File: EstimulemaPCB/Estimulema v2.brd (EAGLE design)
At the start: 150 x 160 mm, 157 parts, among them IC3 74AC14N, IC4 ISO7240S, J1 JUMPERS12MM, J2 J15MM, J3 J_7MM, J4 JUMPERS5MM, J5 JUMPERS7MM, J6 J7MM, K2 HC-06, Q17 TIP48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

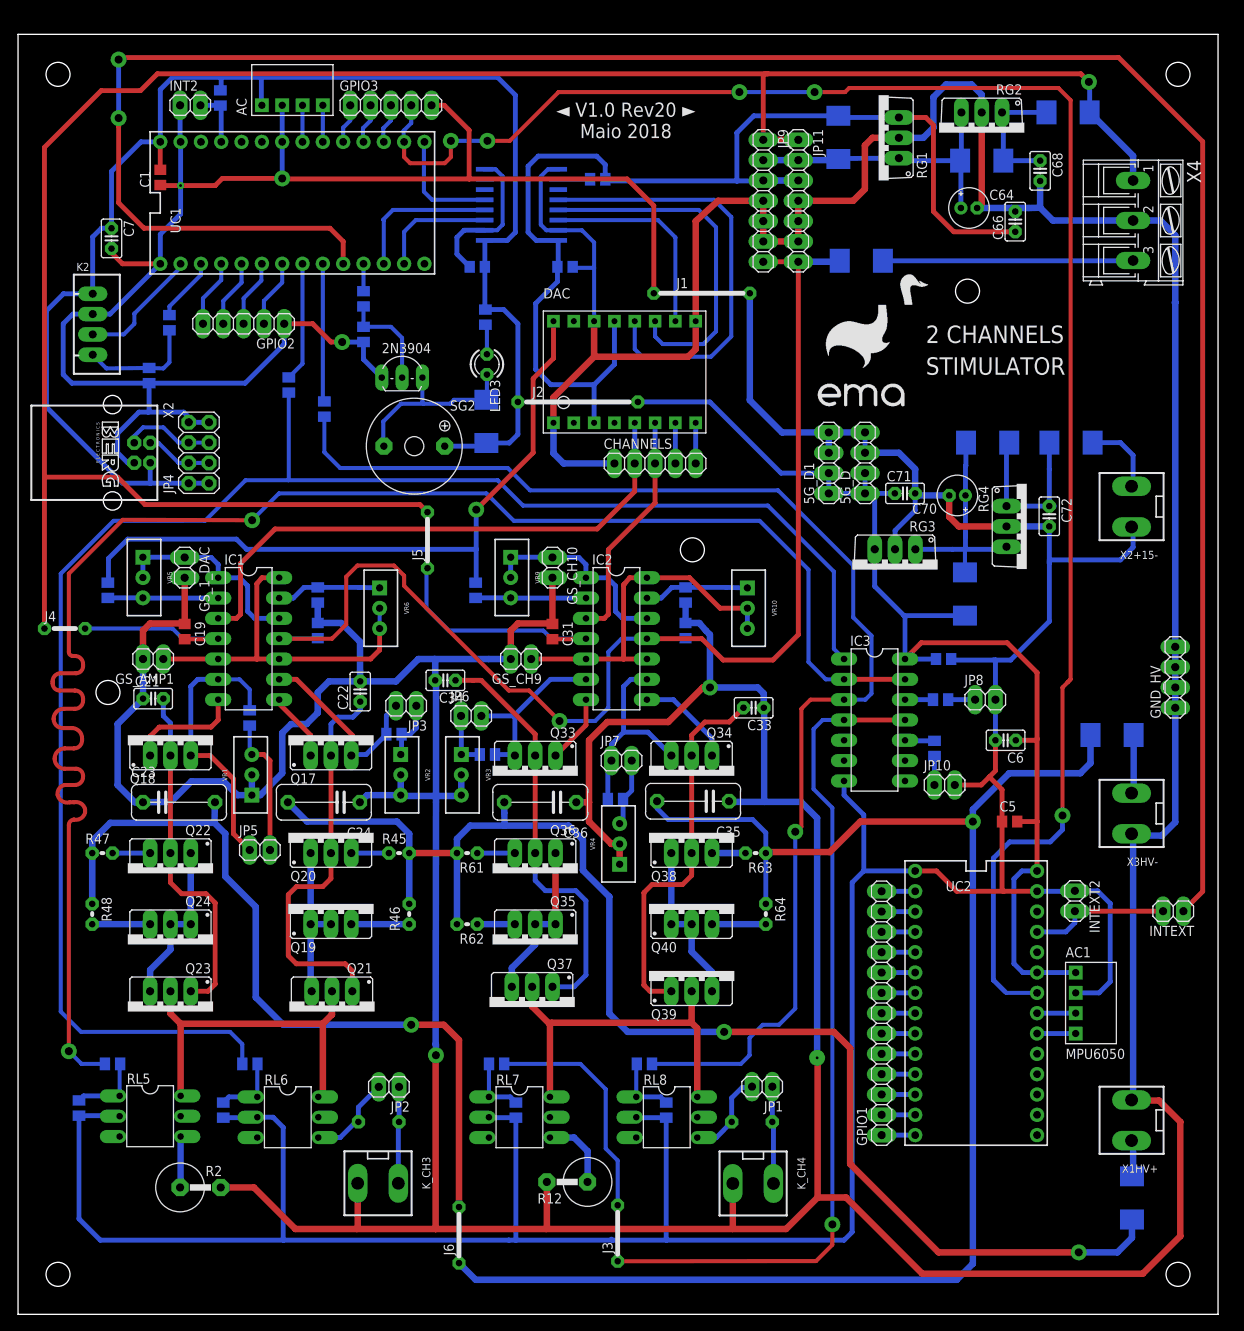
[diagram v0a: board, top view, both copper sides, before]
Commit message: Nueva version del estimulema ino
Version v4 con rampa algunos errores por arreglar
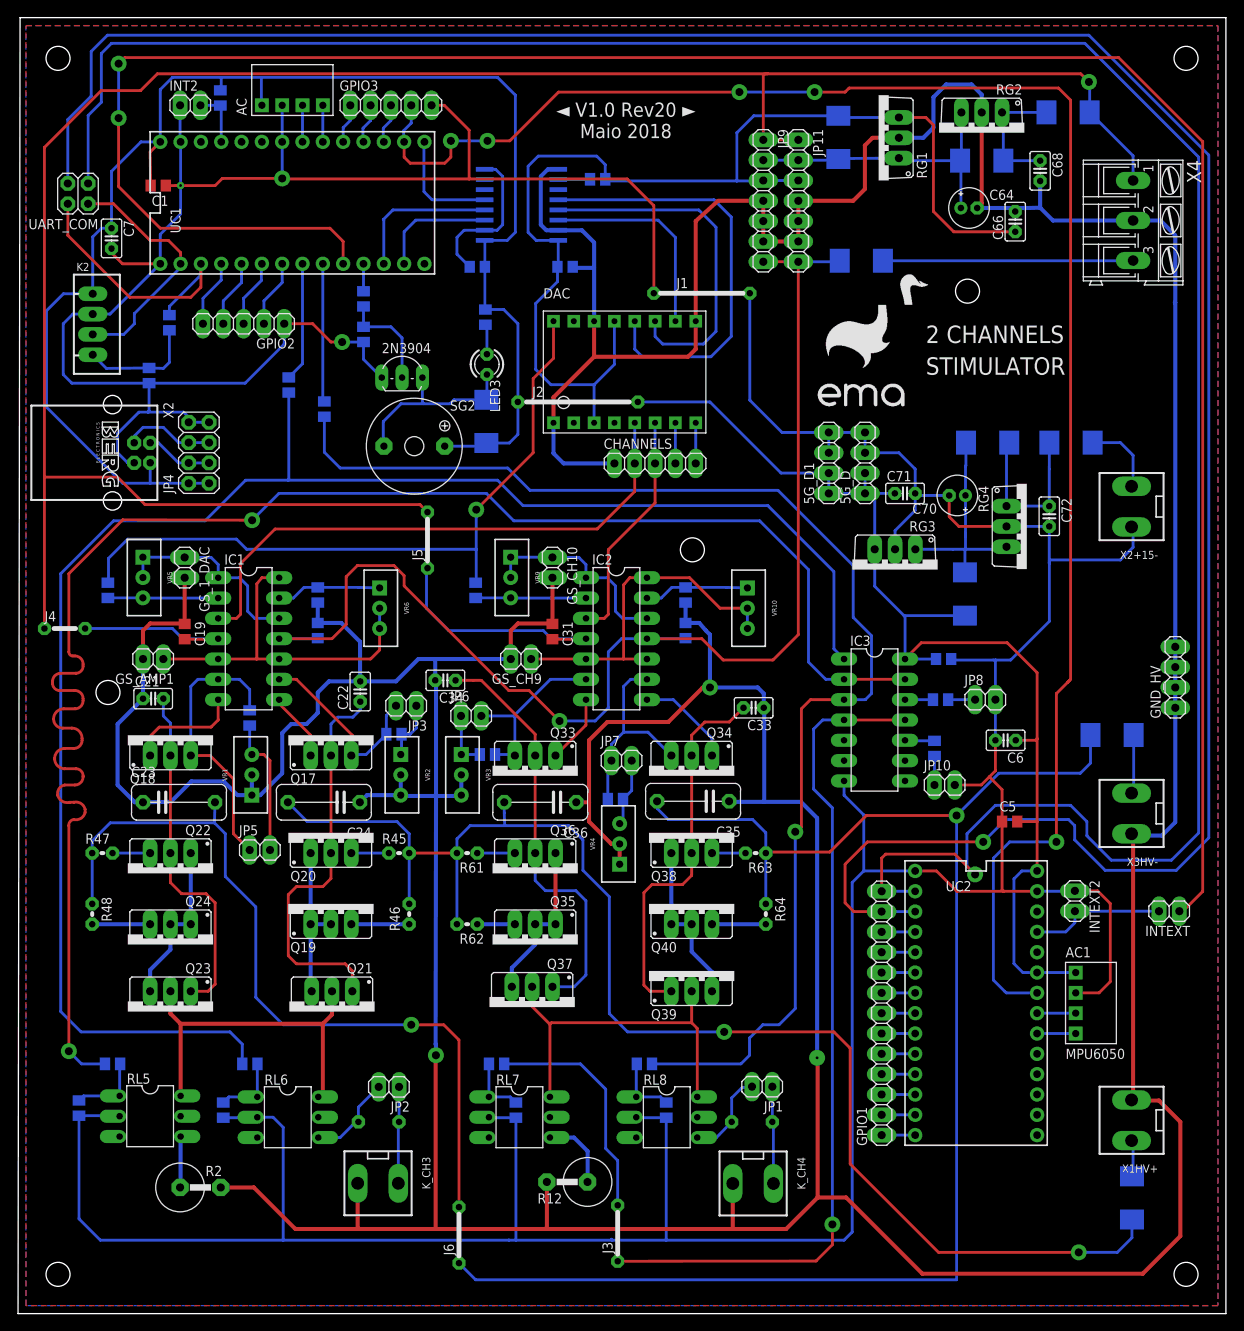
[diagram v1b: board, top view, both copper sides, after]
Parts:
- added UART_COM: (no value), pinhead:2X02
- moved C1 1.05 mm to (18.5, 191.0), turned to 180 degrees
- moved INTEXT 0.51 mm to (144.9, 100.3)
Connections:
- removed net N$70: R16.2, UC1.1
- removed net N$71: K2.3, UC1.0
- new net N$36: R16.2, UART_COM.4, UC1.1
- new net N$38: K2.3, UART_COM.2, UC1.0
- net N$6: now also UART_COM.1
- net N$7: now also UART_COM.3
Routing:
- net N$7: track 4.19 -> 317.0 mm, vias 0 -> 1
- net N$6: track 4.19 -> 307.5 mm, vias 0 -> 1
- net N$36: track 0.00 -> 35.3 mm
- net N$38: track 0.00 -> 31.1 mm
- net N$71: track 15.6 -> 0.00 mm
- net N$70: track 8.05 -> 0.00 mm
- net +5_D: track 336.9 -> 339.4 mm
- net N$5: track 287.9 -> 286.9 mm
- net GND_D: track 646.3 -> 645.6 mm
- net N$1: track 17.9 -> 17.4 mm
- net GND_HV: vias 3 -> 4
- added copper zone on layer 16, net GND_HV
- added copper zone on layer 1, net GND_NV
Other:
- board size 150 x 160 mm -> 151 x 162 mm

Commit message: Actualizacion de PCB
Version corregida con todo
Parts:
- added GPIO2_ACCEL: (no value), pinhead:1X04
- moved D1 8.59 mm to (130.7, 117.5)
- moved C66 1.02 mm to (125.7, 185.5)
- moved R1 0.76 mm to (93.5, 74.0)
- moved K_CH4 0.51 mm to (93.4, 66.3)
- moved C1 0.51 mm to (18.0, 191.0)
- moved K_CH3 0.51 mm to (46.5, 66.3)
- moved R5 0.51 mm to (46.6, 74.0)
- moved JP2 0.51 mm to (47.9, 78.3)
- moved JP1 0.25 mm to (94.3, 78.4)
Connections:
- new net N$37: GPIO2_ACCEL.4, UC2.13
- new net N$39: GPIO2_ACCEL.3, UC2.14/A0
- new net N$40: GPIO2_ACCEL.2, UC2.15/A1
- net N$1: now also GPIO2_ACCEL.1
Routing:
- net N$1: track 17.4 -> 55.4 mm
- net N$40: track 0.00 -> 15.9 mm
- net N$39: track 0.00 -> 11.6 mm
- net HV-: track 294.1 -> 283.0 mm
- net N$37: track 0.00 -> 8.17 mm
- net GND_D: track 645.6 -> 642.5 mm
- net C_CH2: track 162.8 -> 161.2 mm
- net +5_HV: track 143.2 -> 144.5 mm
- net GND_HV: track 815.3 -> 814.0 mm, vias 4 -> 3
- net +15_HV: track 324.6 -> 323.4 mm
- net N$112: track 49.8 -> 48.7 mm
- net 1HV-: track 7.60 -> 8.23 mm
- net N$8: track 11.3 -> 11.8 mm
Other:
- board text added: "◄ V1.0 Rev20 ► Set 2018"
- board text removed: "◄ V1.0 Rev20 ► Maio 2018"

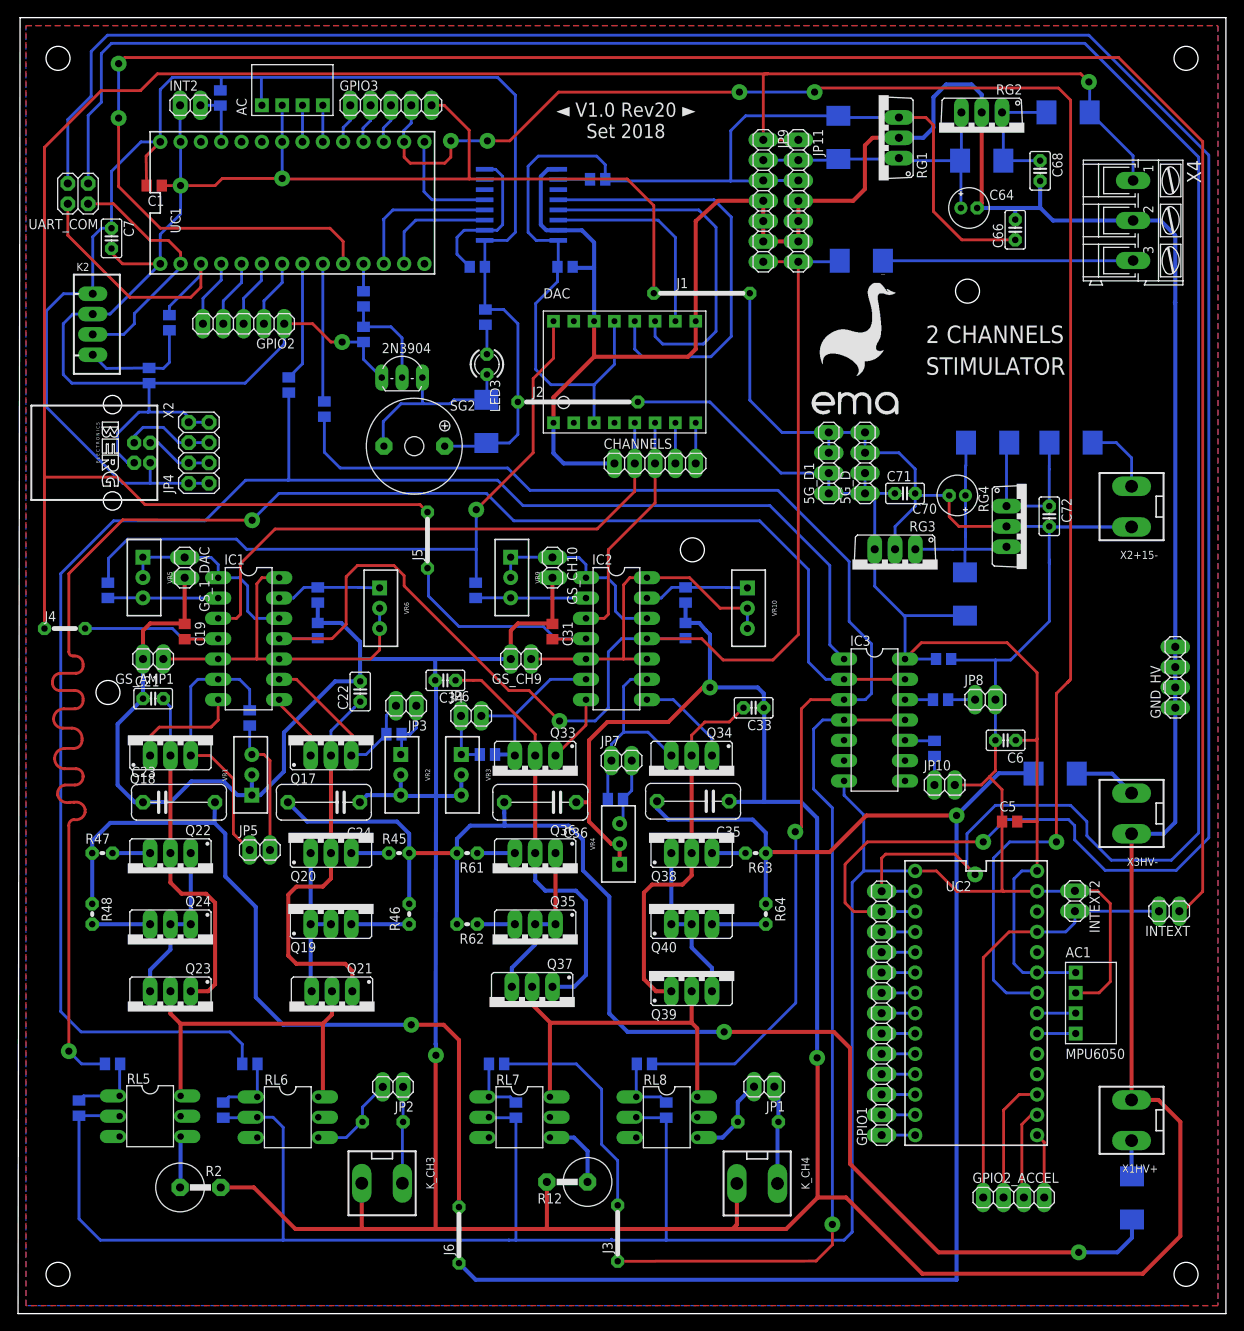
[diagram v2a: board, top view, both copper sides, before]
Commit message: Version final estimulema
con ch1 funcionando con rampa, actualizado pcb y nueva version de estimula a la fecha, ademas de algunos modelos 3d
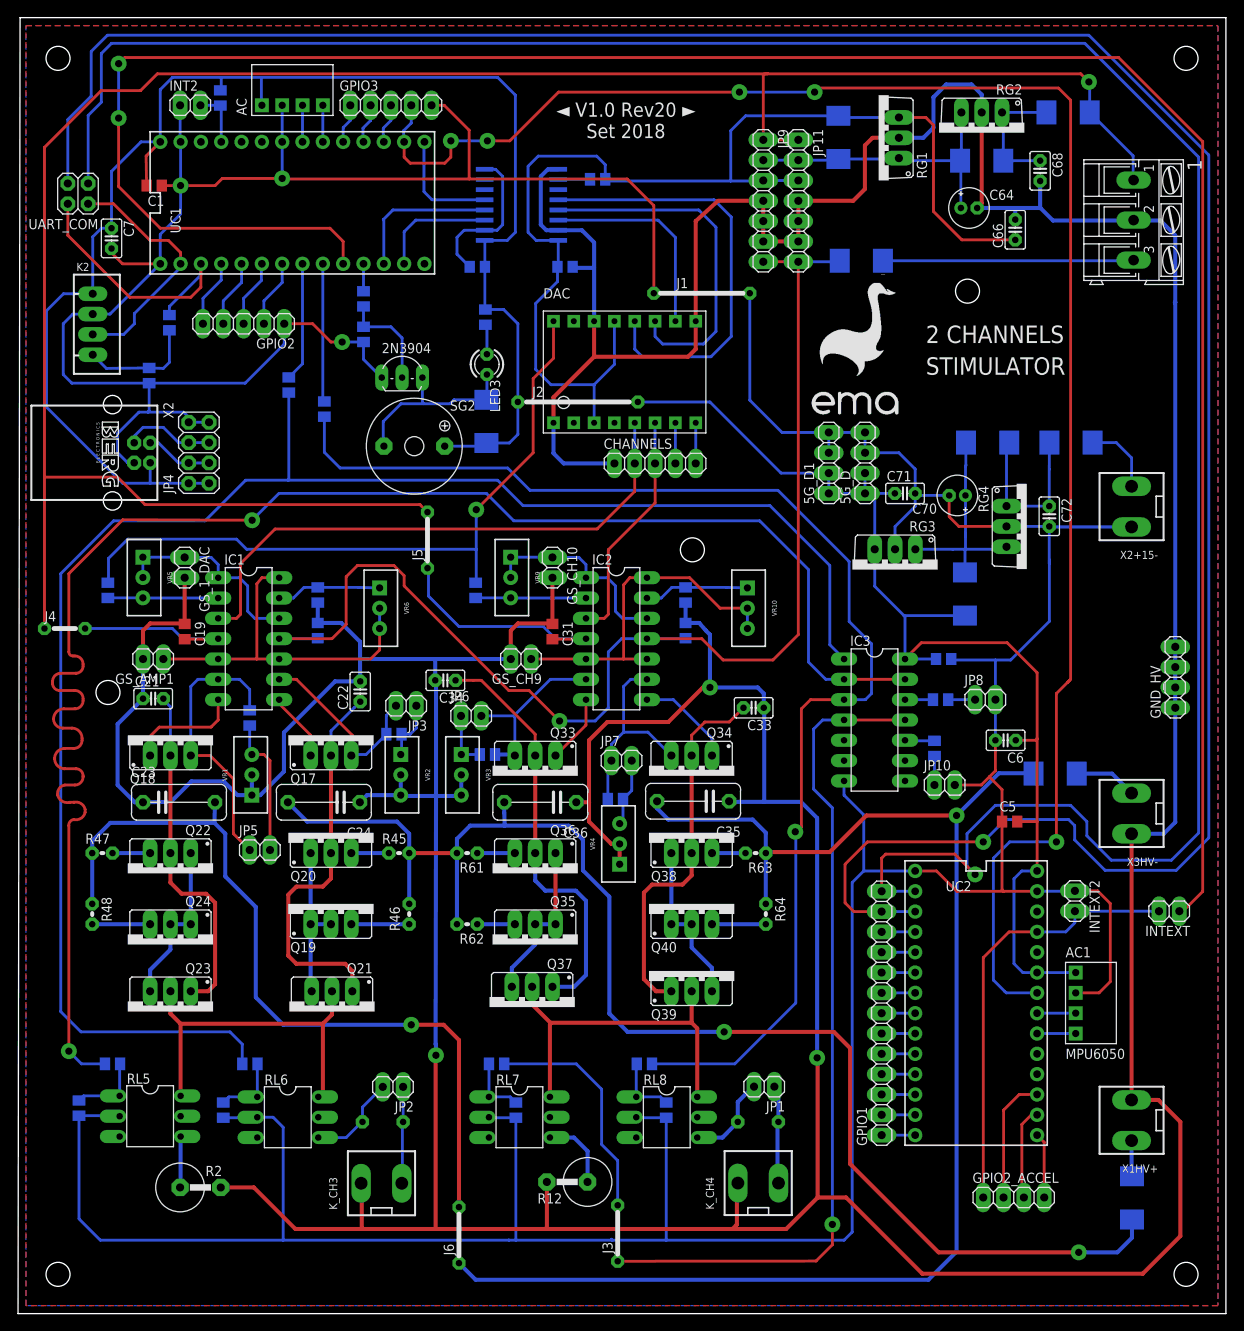
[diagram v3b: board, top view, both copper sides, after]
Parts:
- removed X4: (no value), con-ptr500:AK300/3
- added 1: CONECTOR_3_PTR500, 7DI Library:PTR_AK300/3
- RG1, RG2, RG3, RG4: device linear:TO220V -> 7DI Library:TO220V
- moved K_CH4 0.14 mm to (93.5, 66.3), turned to 0 degrees
- moved K_CH3 0.08 mm to (46.4, 66.3), turned to 0 degrees
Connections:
- net +15_HV: now also 1.1; no longer X4.1
- net -15: now also 1.3; no longer X4.3
- net GND_HV: now also 1.2, K_CH3.1, K_CH4.1; no longer K_CH3.2, K_CH4.2, X4.2
- net N$18: now also K_CH3.2; no longer K_CH3.1
- net N$25: now also K_CH4.2; no longer K_CH4.1
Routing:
- net HV-: track 283.0 -> 280.9 mm

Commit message: update pcb estimulema v2
cerregidos alguns errores que tenia la pcb
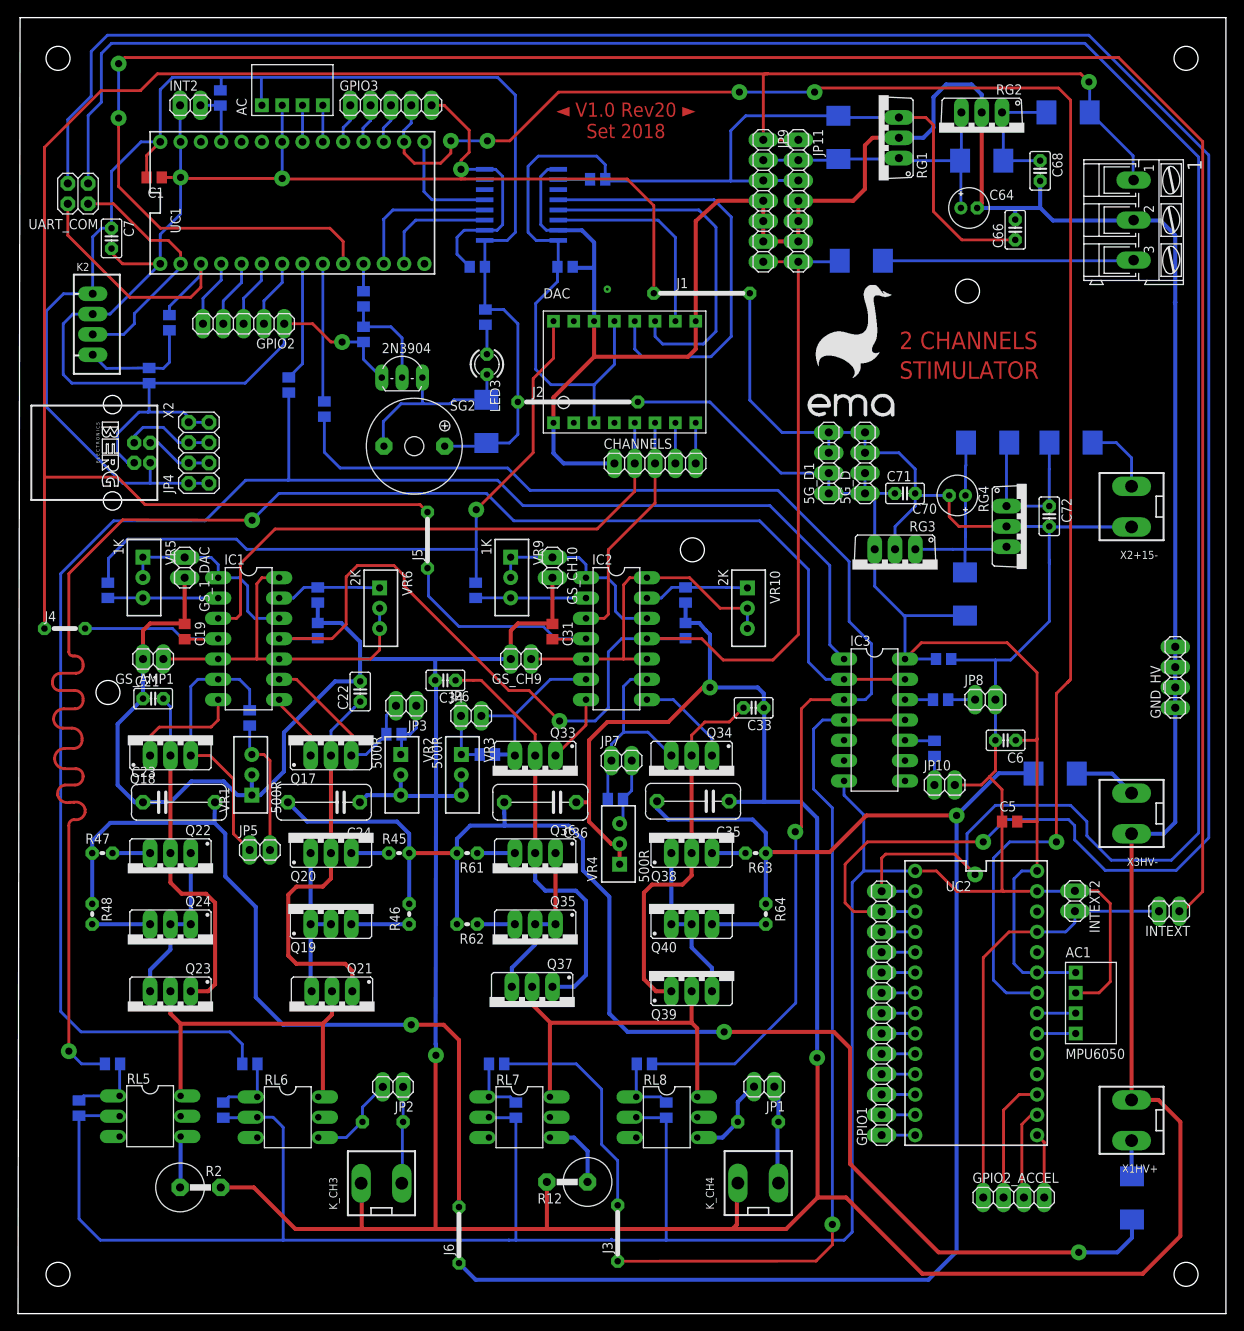
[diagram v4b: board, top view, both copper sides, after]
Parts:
- 1: value CONECTOR_3_PTR500 -> PTR500
- R19: value 1K -> 820r
- R27: value 1K -> 820R
- VR1, VR2, VR3, VR4: value 150R -> 500R
- VR10, VR6: value 2k -> 2K
- VR5, VR9: value TRP -> 1K
- moved C1 1.02 mm to (18.0, 192.0)
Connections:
- removed net GNDI: C3.1, IC4.2, IC4.8
- net GND_D: now also C3.1, IC4.2, IC4.8
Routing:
- net GND_D: track 642.5 -> 665.0 mm, vias 3 -> 4
- net GNDI: track 19.4 -> 0.00 mm
- net +5_D: track 339.6 -> 338.5 mm
- net GPIO5: track 220.1 -> 219.5 mm
- net GND_HV: vias 3 -> 4
- removed copper zone on layer 16, net GND_HV
- removed copper zone on layer 1, net GND_NV
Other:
- board text added: "+15HV"
- board text added: "+8"
- board text added: "-15HV"

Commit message: New version eagle 9.2
arreglando algunas cosas
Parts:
- flipped C1 to the bottom, turned to 0 degrees
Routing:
- net GND_D: track 665.0 -> 669.5 mm
- net +5_D: track 338.5 -> 343.0 mm
- net +8_HV: track 38.6 -> 37.5 mm
- net N$73: track 24.4 -> 23.6 mm
- net N$158: track 22.9 -> 22.3 mm
- net N$145: track 21.1 -> 20.5 mm
- net N$111: track 44.1 -> 43.6 mm
- added copper zone on layer 1, net GND_HV
- added copper zone on layer 16, net GND_HV
